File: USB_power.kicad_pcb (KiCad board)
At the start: 2 copper layers, 45.1 x 66 mm, 31 parts, among them J1 PWR_IN, J2 USB_A_Stacked, J3 Power_check, J4 USB_C_Receptacle_USB2.0_16P, J5 USB_A_Stacked

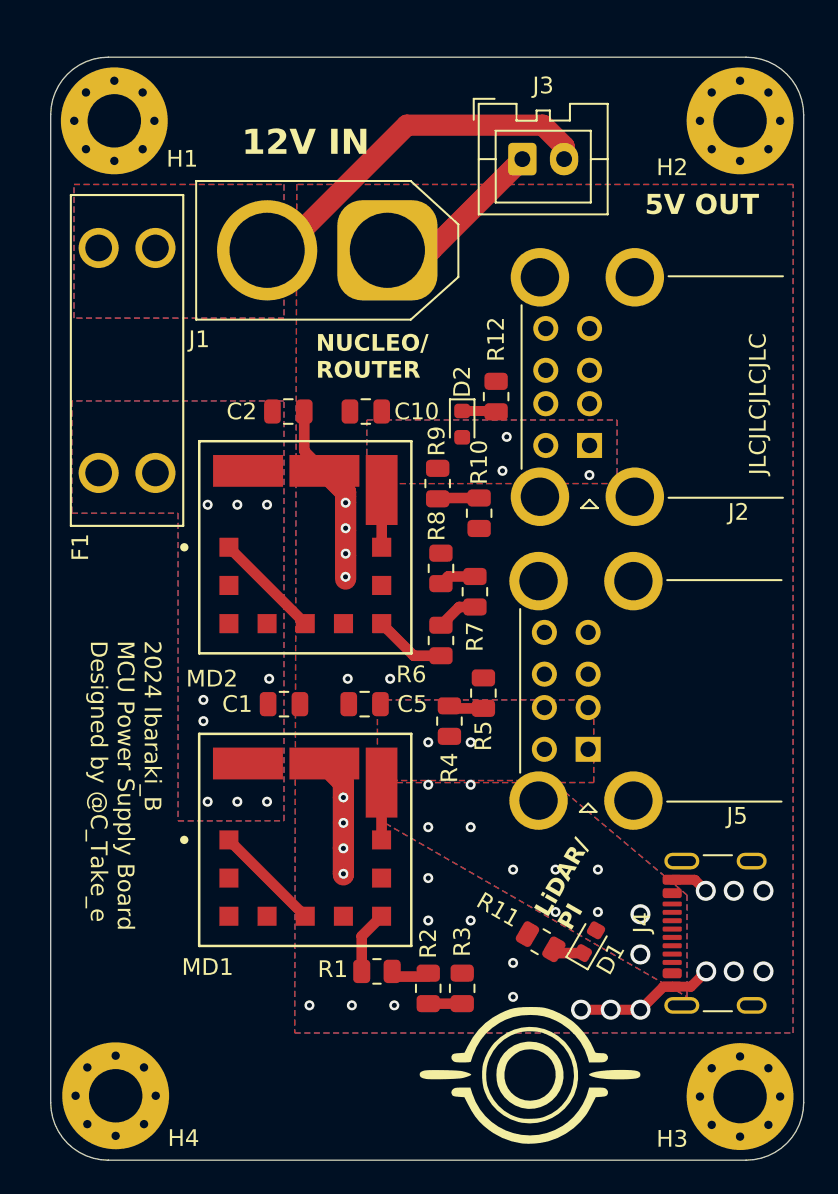
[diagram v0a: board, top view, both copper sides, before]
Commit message: スイッチと分圧抵抗配置
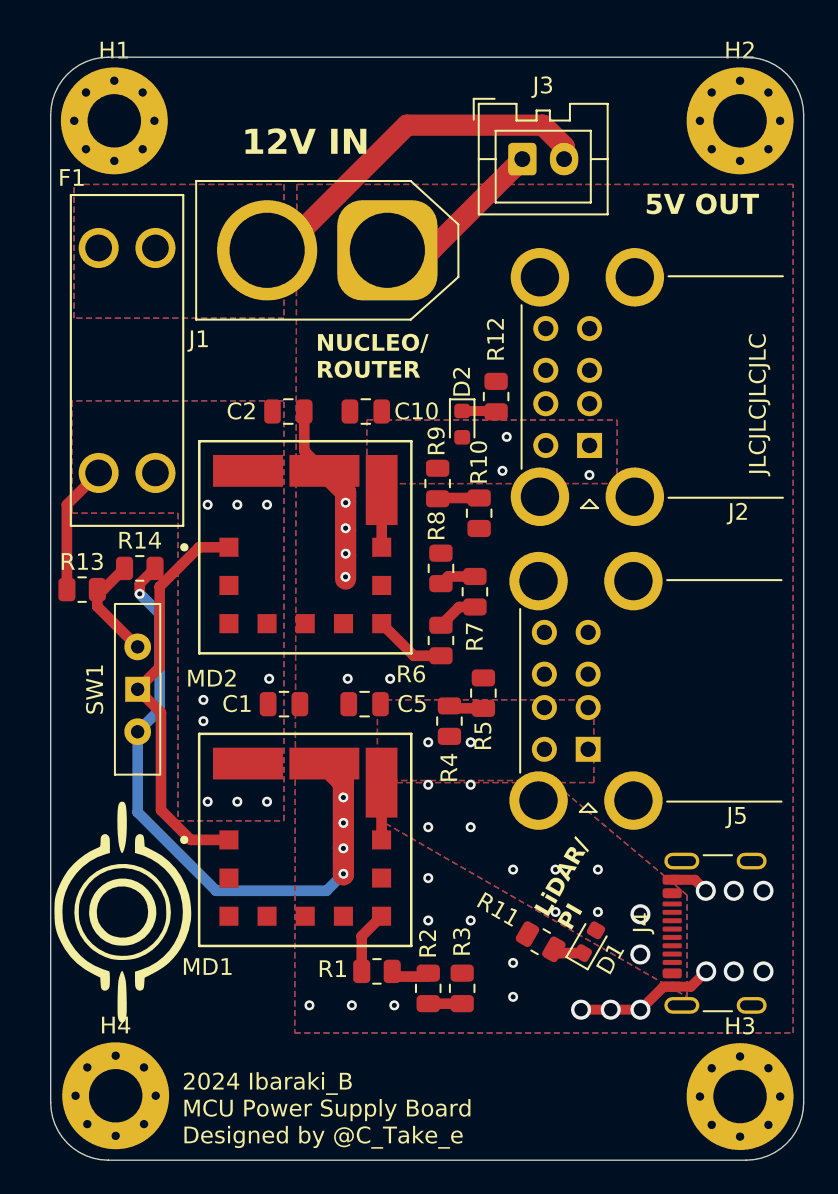
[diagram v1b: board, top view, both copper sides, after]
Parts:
- added R13: 10k, Resistor_SMD:R_0805_2012Metric, F.Cu at (127.6, 103.6)
- added R14: 10k, Resistor_SMD:R_0805_2012Metric, F.Cu at (131.1, 102.4)
- added SW1: Switch, Button_Switch_THT:SW_Slide-03_Wuerth-WS-SLTV_10x2.5x6.4_P2.54mm, F.Cu at (130.9, 109.6)
- moved G*** 26.3 mm to (130.0, 122.9), turned to 90 degrees
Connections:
- MD1 pad 1: GND -> CTRL
- MD2 pad 1: GND -> CTRL
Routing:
- net CTRL: track 0.00 -> 24.4 mm
- net GND: track 52.5 -> 75.2 mm, vias 27 -> 28
- net Battery: track 0.00 -> 7.77 mm
- net Net-(SW1-A): track 0.00 -> 6.58 mm

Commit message: スイッチ回り配線改善
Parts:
- removed the G*** at (130.0, 122.9)
- added G***: LOGO, USB_power:HALO_small, F.Cu at (158.0, 133.6)
- moved SW1 5.40 mm to (128.3, 114.3)
- moved R14 4.54 mm to (129.0, 106.4)
- moved R13 1.03 mm to (127.8, 102.6)
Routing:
- net CTRL: track 24.4 -> 28.8 mm
- net Net-(SW1-A): track 6.58 -> 9.44 mm
- net GND: track 75.2 -> 73.4 mm
- net Battery: track 7.77 -> 6.82 mm, vias 9 -> 18

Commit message: DRC実行！！！！！！
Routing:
- net Battery: vias 18 -> 21
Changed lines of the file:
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@@
+	)
+	(via
+		(at 128.778 93.218)
+		(size 0.6)
+		(drill 0.3)
+		(layers "F.Cu" "B.Cu")
+		(free yes)
+		(net 53)
 	)
 	(via
@@
 	(via
 		(at 138.684 103.759)
+		(size 0.6)
+		(drill 0.3)
+		(layers "F.Cu" "B.Cu")
+		(free yes)
+		(net 53)
+	)
+	(via
+		(at 130.81 93.218)
 		(size 0.6)
 		(drill 0.3)
@@
 		(size 0.6)
 		(drill 0.3)
+		(layers "F.Cu" "B.Cu")
+		(free yes)
+		(net 53)
+	)
+	(via
+		(at 132.842 93.218)
+		(size 0.6)
+		(drill 0.3)
